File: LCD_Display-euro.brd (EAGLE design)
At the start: 41.9 x 30.5 mm, 4 parts, among them U1 NEWHAVEN_LCD

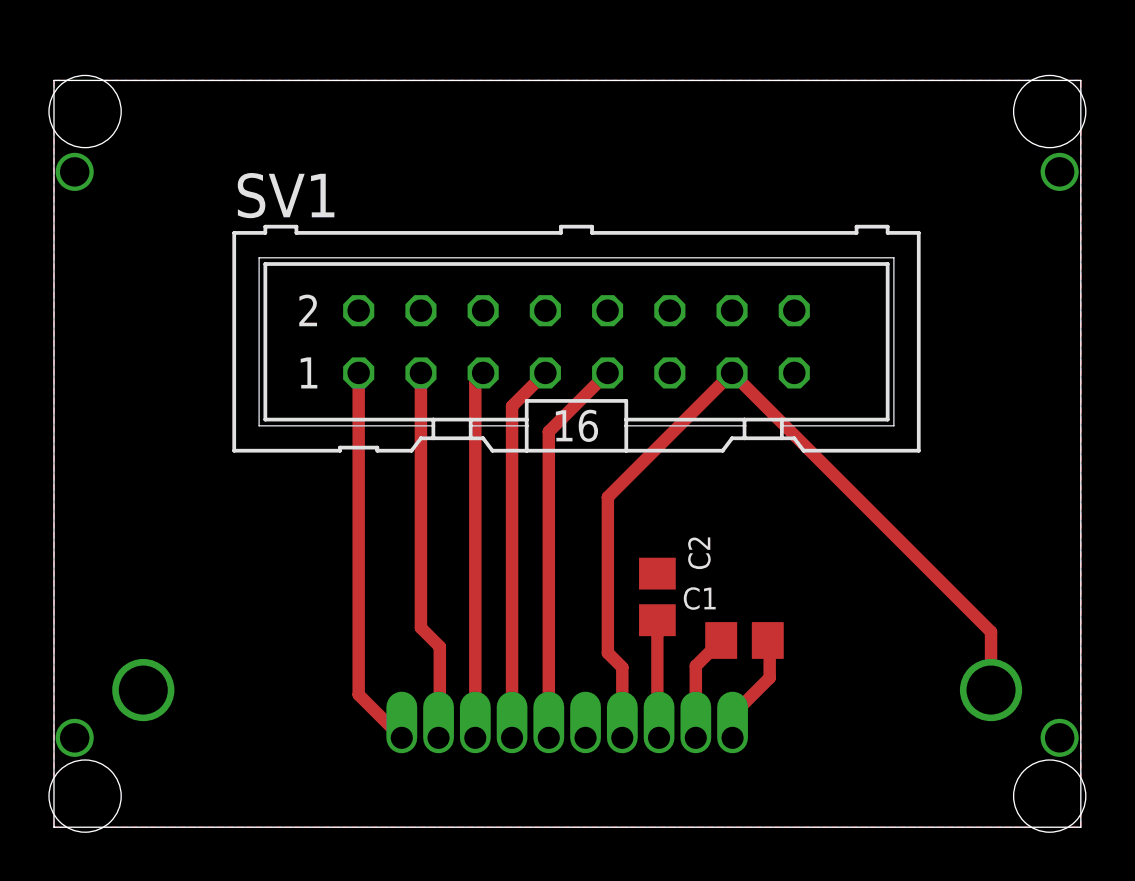
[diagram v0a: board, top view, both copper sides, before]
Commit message: Tweaked hole spacing; exported gerbers for LCD_Display Euro
Sized for 12HP Eurocard module
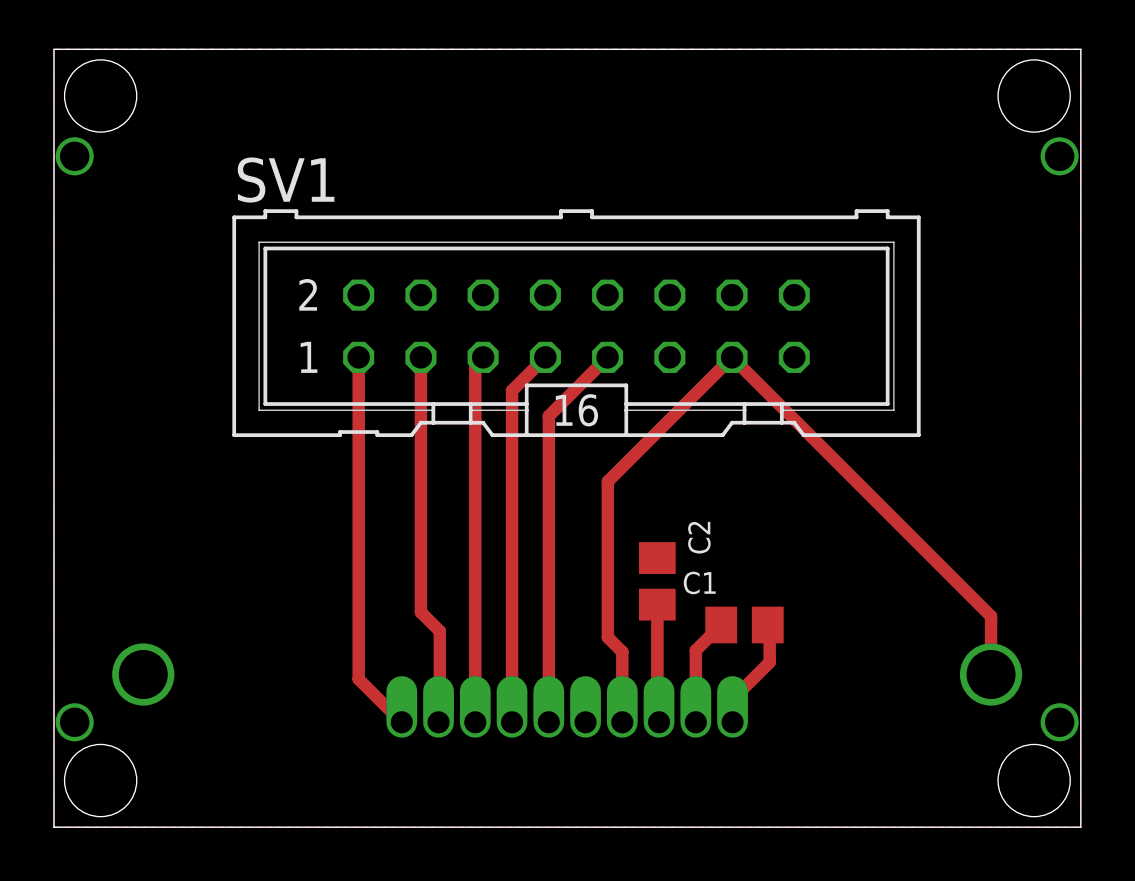
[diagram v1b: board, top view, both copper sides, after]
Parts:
- moved C1 0.64 mm to (28.2, 8.26)
- moved C2 0.63 mm to (24.6, 10.0)
- moved U1 0.63 mm to (41.6, 3.68)
- moved SV1 0.63 mm to (21.3, 20.4)
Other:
- board size 41.9 x 30.5 mm -> 41.9 x 31.8 mm
- board text added: "Sized for 12HP Eurocard unit"
- board text removed: "Sized for Eurocard unit"

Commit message: Fixed up Eurocard LCD module for production run
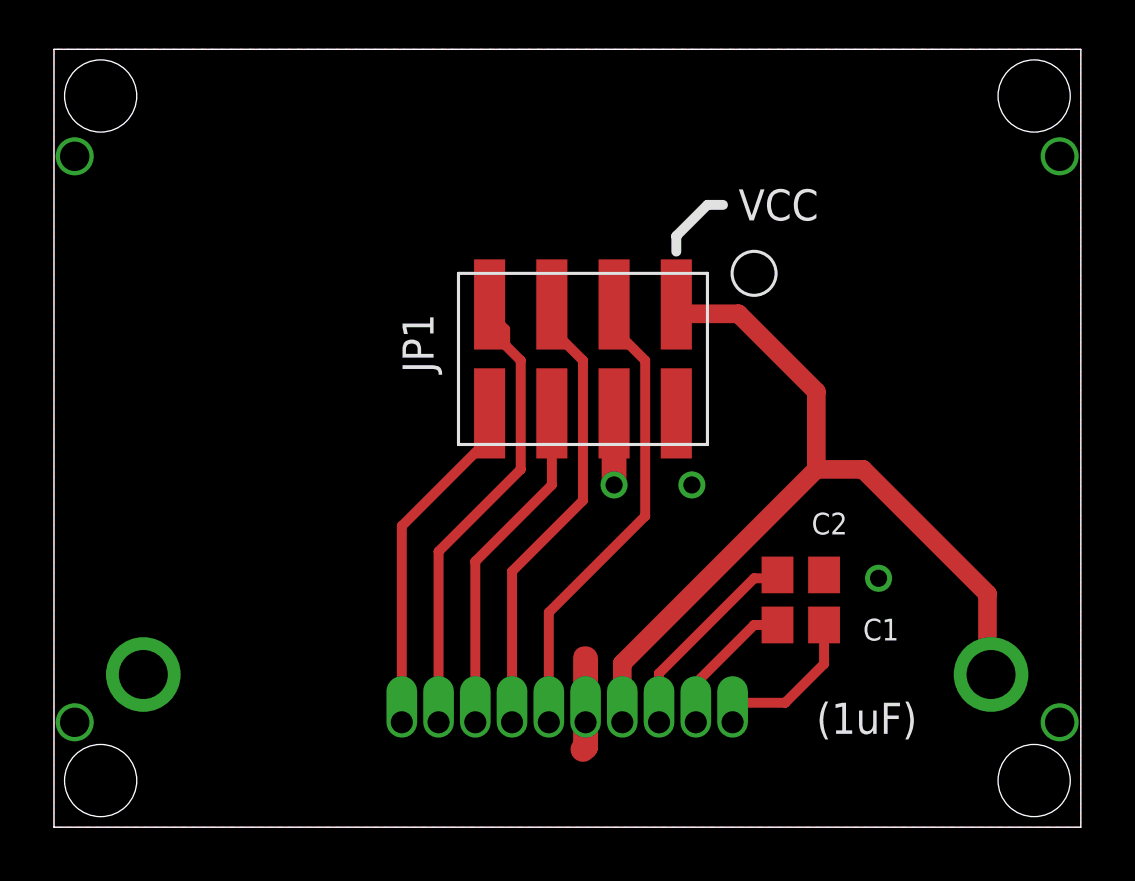
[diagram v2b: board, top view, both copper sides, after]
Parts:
- removed SV1: Ribbon Header, mcu-accessories:ML16
- added JP1: (no value), mcu-accessories:2X4SMT
- moved C2 5.86 mm to (30.5, 10.3), turned to 180 degrees
- moved C1 2.30 mm to (30.5, 8.26)
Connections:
- net CSB: now also JP1.6; no longer SV1.5
- net GND: now also JP1.2, JP1.4; no longer SV1.11
- net RS: now also JP1.7; no longer SV1.3
- net RST: now also JP1.8; no longer SV1.1
- net SCL: now also JP1.5; no longer SV1.7
- net SI: now also JP1.3; no longer SV1.9
- net VDD: now also JP1.1; no longer SV1.13
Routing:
- net GND: track 0.00 -> 5.80 mm, vias 0 -> 3
- net RS: track 15.2 -> 19.0 mm
- net N$3: track 4.83 -> 8.50 mm
- net SCL: track 15.5 -> 18.8 mm
- net SI: track 15.9 -> 19.2 mm
- net N$2: track 4.63 -> 6.63 mm
- net VDD: track 34.6 -> 36.4 mm
- net N$1: track 4.40 -> 6.23 mm
- net RST: track 15.6 -> 14.1 mm
- net CSB: track 15.0 -> 13.9 mm
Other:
- board text added: "(1uF)"
- board text added: "VCC"

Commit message: Rotated connector on LCD display for eurocard
I believe it should still be rotated 180 degrees to match IDC cable
orientation better.
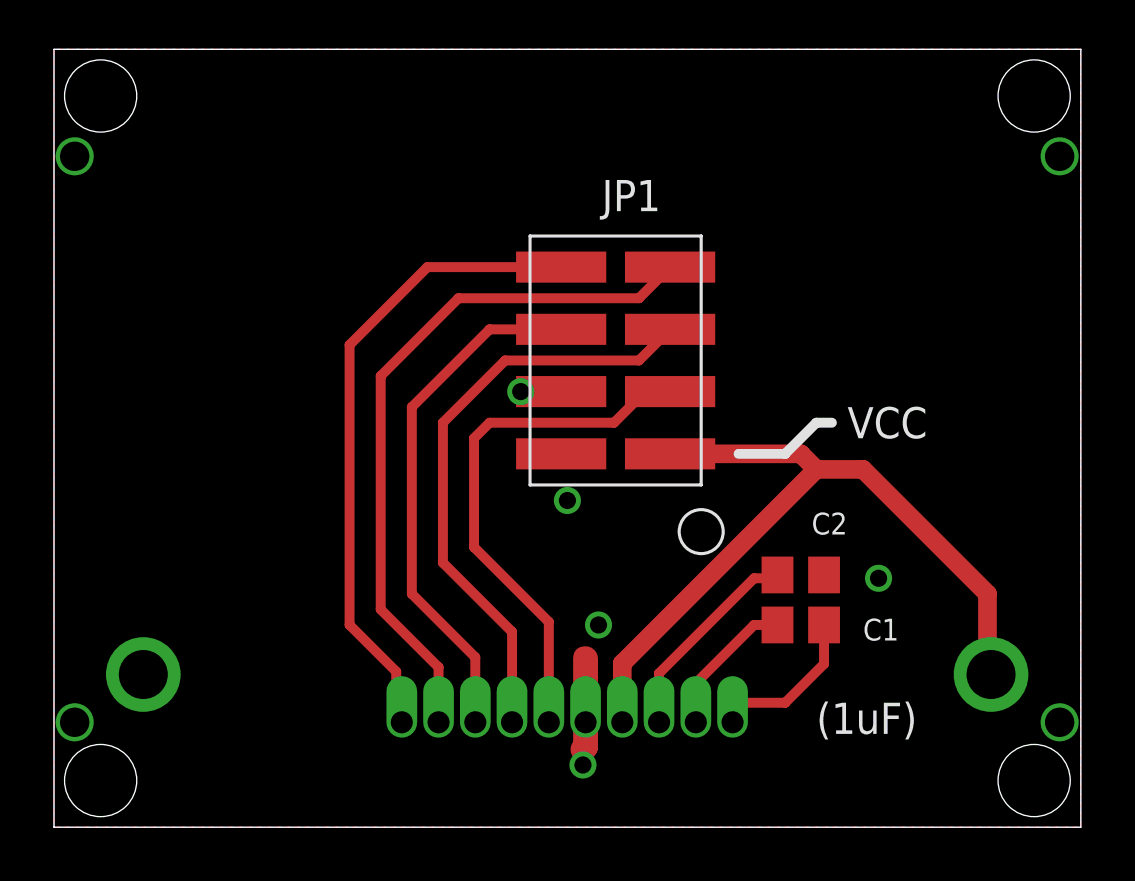
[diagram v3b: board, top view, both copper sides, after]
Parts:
- moved JP1 1.27 mm to (22.9, 19.1), turned to 90 degrees
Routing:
- net RST: track 14.1 -> 26.2 mm
- net RS: track 19.0 -> 28.8 mm
- net CSB: track 13.9 -> 21.3 mm
- net SCL: track 18.8 -> 24.2 mm
- net VDD: track 36.4 -> 32.3 mm
- net SI: track 19.2 -> 21.6 mm
- net GND: track 5.80 -> 3.90 mm, vias 3 -> 5
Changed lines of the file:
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@@
 <dimension x1="40.005" y1="1.905" x2="41.275" y2="11.43" x3="40.64" y3="-2.54" textsize="1.778" layer="48" dtype="horizontal" unit="inch"/>
 <dimension x1="41.275" y1="-2.54" x2="0.635" y2="12.065" x3="20.955" y3="-6.985" textsize="1.778" layer="48" dtype="horizontal" unit="inch"/>
-<text x="27.94" y="24.765" size="1.27" layer="21">VCC</text>
-<wire x1="27.305" y1="25.4" x2="26.67" y2="25.4" width="0.4064" layer="21"/>
-<wire x1="26.67" y1="25.4" x2="25.4" y2="24.13" width="0.4064" layer="21"/>
-<wire x1="25.4" y1="24.13" x2="25.4" y2="23.495" width="0.4064" layer="21"/>
+<text x="32.385" y="15.875" size="1.27" layer="21">VCC</text>
+<wire x1="31.75" y1="16.51" x2="31.115" y2="16.51" width="0.4064" layer="21"/>
+<wire x1="31.115" y1="16.51" x2="29.845" y2="15.24" width="0.4064" layer="21"/>
+<wire x1="29.845" y1="15.24" x2="27.94" y2="15.24" width="0.4064" layer="21"/>
 <text x="31.115" y="3.81" size="1.27" layer="21">(1uF)</text>
 </plain>
@@
 <attribute name="VALUE" x="33.02" y="12.202" size="0.889" layer="27" rot="R180"/>
 </element>
-<element name="JP1" library="mcu-accessories" package="2X4SMT" value="" x="21.59" y="19.05" smashed="yes" rot="R180">
-<attribute name="NAME" x="14.224" y="20.955" size="1.27" layer="21" rot="R270"/>
+<element name="JP1" library="mcu-accessories" package="2X4SMT" value="" x="22.86" y="19.05" smashed="yes" rot="R90">
+<attribute name="NAME" x="24.765" y="26.416" size="1.27" layer="21" rot="R180"/>
 </element>
 </elements>
@@
 <contactref element="JP1" pad="2"/>
 <contactref element="JP1" pad="4"/>
-<via x="22.86" y="13.97" extent="1-16" drill="0.7"/>
-<via x="26.035" y="13.97" extent="1-16" drill="0.7"/>
+<via x="20.955" y="13.335" extent="1-16" drill="0.7"/>
+<via x="22.225" y="8.255" extent="1-16" drill="0.7"/>
 <via x="33.655" y="10.16" extent="1-16" drill="0.7"/>
 <wire x1="21.696" y1="6.879" x2="21.59" y2="6.985" width="0.762" layer="1"/>
-<wire x1="22.86" y1="13.97" x2="22.86" y2="15.875" width="1.016" layer="1"/>
 <wire x1="21.696" y1="4.283" x2="21.696" y2="6.879" width="1.016" layer="1"/>
 <wire x1="21.696" y1="4.283" x2="21.696" y2="3.281" width="1.016" layer="1"/>
 <wire x1="21.696" y1="3.281" x2="21.59" y2="3.175" width="1.016" layer="1"/>
+<via x="19.05" y="17.78" extent="1-16" drill="0.7"/>
+<via x="21.59" y="2.54" extent="1-16" drill="0.7"/>
 </signal>
 <signal name="VDD">
@@
 <wire x1="23.196" y1="4.283" x2="23.196" y2="6.686" width="0.762" layer="1"/>
 <wire x1="23.196" y1="6.686" x2="31.115" y2="14.605" width="0.762" layer="1"/>
-<wire x1="31.115" y1="14.605" x2="31.115" y2="17.78" width="0.762" layer="1"/>
-<wire x1="31.115" y1="17.78" x2="27.94" y2="20.955" width="0.762" layer="1"/>
-<wire x1="27.94" y1="20.955" x2="25.781" y2="20.955" width="0.762" layer="1"/>
-<wire x1="25.781" y1="20.955" x2="25.4" y2="21.336" width="0.762" layer="1"/>
 <wire x1="31.115" y1="14.605" x2="33.02" y2="14.605" width="0.762" layer="1"/>
 <wire x1="33.02" y1="14.605" x2="38.1" y2="9.525" width="0.762" layer="1"/>
 <wire x1="38.1" y1="9.525" x2="38.1" y2="6.379" width="0.762" layer="1"/>
 <wire x1="38.1" y1="6.379" x2="38.246" y2="6.233" width="0.762" layer="1"/>
+<wire x1="25.146" y1="15.24" x2="30.48" y2="15.24" width="0.762" layer="1"/>
+<wire x1="30.48" y1="15.24" x2="31.115" y2="14.605" width="0.762" layer="1"/>
 </signal>
 <signal name="SI">
 <contactref element="U1" pad="5"/>
 <contactref element="JP1" pad="3"/>
-<wire x1="20.196" y1="4.283" x2="20.196" y2="8.766" width="0.4064" layer="1"/>
-<wire x1="20.196" y1="8.766" x2="24.13" y2="12.7" width="0.4064" layer="1"/>
-<wire x1="24.13" y1="12.7" x2="24.13" y2="19.05" width="0.4064" layer="1"/>
-<wire x1="24.13" y1="19.05" x2="22.86" y2="20.32" width="0.4064" layer="1"/>
-<wire x1="22.86" y1="20.32" x2="22.86" y2="21.336" width="0.4064" layer="1"/>
+<wire x1="25.146" y1="17.78" x2="24.13" y2="17.78" width="0.4064" layer="1"/>
+<wire x1="24.13" y1="17.78" x2="22.86" y2="16.51" width="0.4064" layer="1"/>
+<wire x1="22.86" y1="16.51" x2="17.78" y2="16.51" width="0.4064" layer="1"/>
+<wire x1="17.78" y1="16.51" x2="17.145" y2="15.875" width="0.4064" layer="1"/>
+<wire x1="17.145" y1="15.875" x2="17.145" y2="11.43" width="0.4064" layer="1"/>
+<wire x1="17.145" y1="11.43" x2="20.196" y2="8.379" width="0.4064" layer="1"/>
+<wire x1="20.196" y1="8.379" x2="20.196" y2="4.283" width="0.4064" layer="1"/>
 </signal>
 <signal name="SCL">
 <contactref element="U1" pad="4"/>
 <contactref element="JP1" pad="5"/>
-<wire x1="18.696" y1="4.283" x2="18.696" y2="10.441" width="0.4064" layer="1"/>
-<wire x1="18.696" y1="10.441" x2="21.59" y2="13.335" width="0.4064" layer="1"/>
-<wire x1="21.59" y1="13.335" x2="21.59" y2="19.05" width="0.4064" layer="1"/>
-<wire x1="21.59" y1="19.05" x2="20.32" y2="20.32" width="0.4064" layer="1"/>
-<wire x1="20.32" y1="20.32" x2="20.32" y2="21.336" width="0.4064" layer="1"/>
+<wire x1="18.696" y1="4.283" x2="18.696" y2="7.974" width="0.4064" layer="1"/>
+<wire x1="18.415" y1="19.05" x2="23.876" y2="19.05" width="0.4064" layer="1"/>
+<wire x1="23.876" y1="19.05" x2="25.146" y2="20.32" width="0.4064" layer="1"/>
+<wire x1="18.696" y1="7.974" x2="15.875" y2="10.795" width="0.4064" layer="1"/>
+<wire x1="15.875" y1="10.795" x2="15.875" y2="16.51" width="0.4064" layer="1"/>
+<wire x1="15.875" y1="16.51" x2="18.415" y2="19.05" width="0.4064" layer="1"/>
 </signal>
 <signal name="CSB">
 <contactref element="U1" pad="3"/>
 <contactref element="JP1" pad="6"/>
-<wire x1="17.196" y1="4.283" x2="17.196" y2="10.846" width="0.4064" layer="1"/>
-<wire x1="17.196" y1="10.846" x2="20.32" y2="13.97" width="0.4064" layer="1"/>
-<wire x1="20.32" y1="13.97" x2="20.32" y2="16.891" width="0.4064" layer="1"/>
+<wire x1="20.701" y1="20.32" x2="17.78" y2="20.32" width="0.4064" layer="1"/>
+<wire x1="17.196" y1="6.934" x2="17.196" y2="4.283" width="0.4064" layer="1"/>
+<wire x1="17.78" y1="20.32" x2="14.605" y2="17.145" width="0.4064" layer="1"/>
+<wire x1="14.605" y1="17.145" x2="14.605" y2="9.525" width="0.4064" layer="1"/>
+<wire x1="14.605" y1="9.525" x2="17.196" y2="6.934" width="0.4064" layer="1"/>
 </signal>
 <signal name="RS">
 <contactref element="U1" pad="2"/>
 <contactref element="JP1" pad="7"/>
-<wire x1="15.696" y1="4.283" x2="15.696" y2="11.251" width="0.4064" layer="1"/>
-<wire x1="15.696" y1="11.251" x2="19.05" y2="14.605" width="0.4064" layer="1"/>
-<wire x1="19.05" y1="14.605" x2="19.05" y2="19.05" width="0.4064" layer="1"/>
-<wire x1="19.05" y1="19.05" x2="18.415" y2="19.685" width="0.4064" layer="1"/>
-<wire x1="18.415" y1="19.685" x2="18.415" y2="20.32" width="0.4064" layer="1"/>
-<wire x1="18.415" y1="20.32" x2="17.78" y2="20.955" width="0.4064" layer="1"/>
-<wire x1="17.78" y1="20.955" x2="17.78" y2="21.336" width="0.4064" layer="1"/>
+<wire x1="25.146" y1="22.86" x2="23.876" y2="21.59" width="0.4064" layer="1"/>
+<wire x1="23.876" y1="21.59" x2="16.51" y2="21.59" width="0.4064" layer="1"/>
+<wire x1="16.51" y1="21.59" x2="13.335" y2="18.415" width="0.4064" layer="1"/>
+<wire x1="13.335" y1="18.415" x2="13.335" y2="8.89" width="0.4064" layer="1"/>
+<wire x1="13.335" y1="8.89" x2="15.696" y2="6.529" width="0.4064" layer="1"/>
+<wire x1="15.696" y1="6.529" x2="15.696" y2="4.283" width="0.4064" layer="1"/>
 </signal>
 <signal name="RST">
 <contactref element="U1" pad="1"/>
 <contactref element="JP1" pad="8"/>
-<wire x1="14.196" y1="4.283" x2="14.196" y2="12.291" width="0.4064" layer="1"/>
-<wire x1="14.196" y1="12.291" x2="17.78" y2="15.875" width="0.4064" layer="1"/>
-<wire x1="17.78" y1="15.875" x2="17.78" y2="16.891" width="0.4064" layer="1"/>
+<wire x1="15.24" y1="22.86" x2="20.701" y2="22.86" width="0.4064" layer="1"/>
+<wire x1="14.196" y1="4.283" x2="13.97" y2="4.509" width="0.4064" layer="1"/>
+<wire x1="13.97" y1="4.509" x2="13.97" y2="6.35" width="0.4064" layer="1"/>
+<wire x1="13.97" y1="6.35" x2="12.065" y2="8.255" width="0.4064" layer="1"/>
+<wire x1="12.065" y1="8.255" x2="12.065" y2="19.685" width="0.4064" layer="1"/>
+<wire x1="12.065" y1="19.685" x2="15.24" y2="22.86" width="0.4064" layer="1"/>
 </signal>
 </signals>
